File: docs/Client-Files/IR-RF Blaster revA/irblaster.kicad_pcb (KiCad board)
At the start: 2 copper layers, 65 x 61 mm, 68 parts, among them J1 VoltLink_target, J2 TYPE-C-31-M-17, Q1 YJL2302B, SW1 USER, U1 ESP32-S3-WROOM-1U-N4, U2 IRM-H638T/TR2, U3 IRM-3638T, U4 LR1107, U5 E07-400M10S

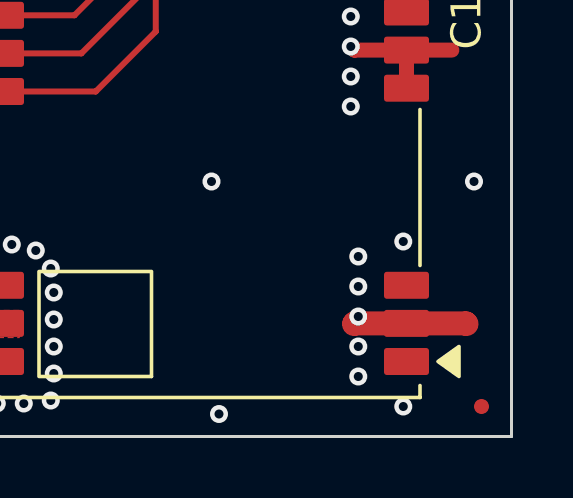
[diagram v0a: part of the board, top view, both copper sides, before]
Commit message: through hole Test point and overlay update
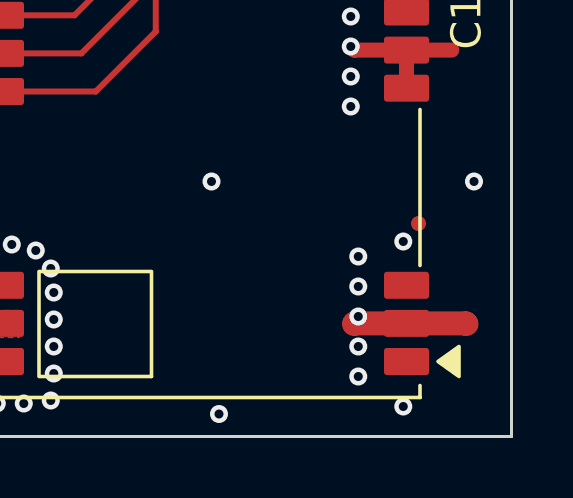
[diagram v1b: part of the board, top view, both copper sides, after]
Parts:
- moved FID3 6.45 mm to (152.4, 152.4)
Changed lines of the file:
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@@
   )
   (footprint "Fiducial:Fiducial_0.5mm_Mask1mm" (layer "F.Cu")
-    (at 154.5 158.5)
+    (at 152.4 152.4)
     (descr "Circular Fiducial, 0.5mm bare copper, 1mm soldermask opening (Level C)")
     (tags "fiducial")
